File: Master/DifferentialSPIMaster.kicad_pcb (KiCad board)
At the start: 4 copper layers, 36 parts, among them J1 Motor Encoder 0, J2 Conn_01x20, J3 Motor Encoder 0, U1 MAX485E, U2 MAX485E, U3 MAX485E, U4 MAX485E, U5 MAX485E, U6 MAX485E

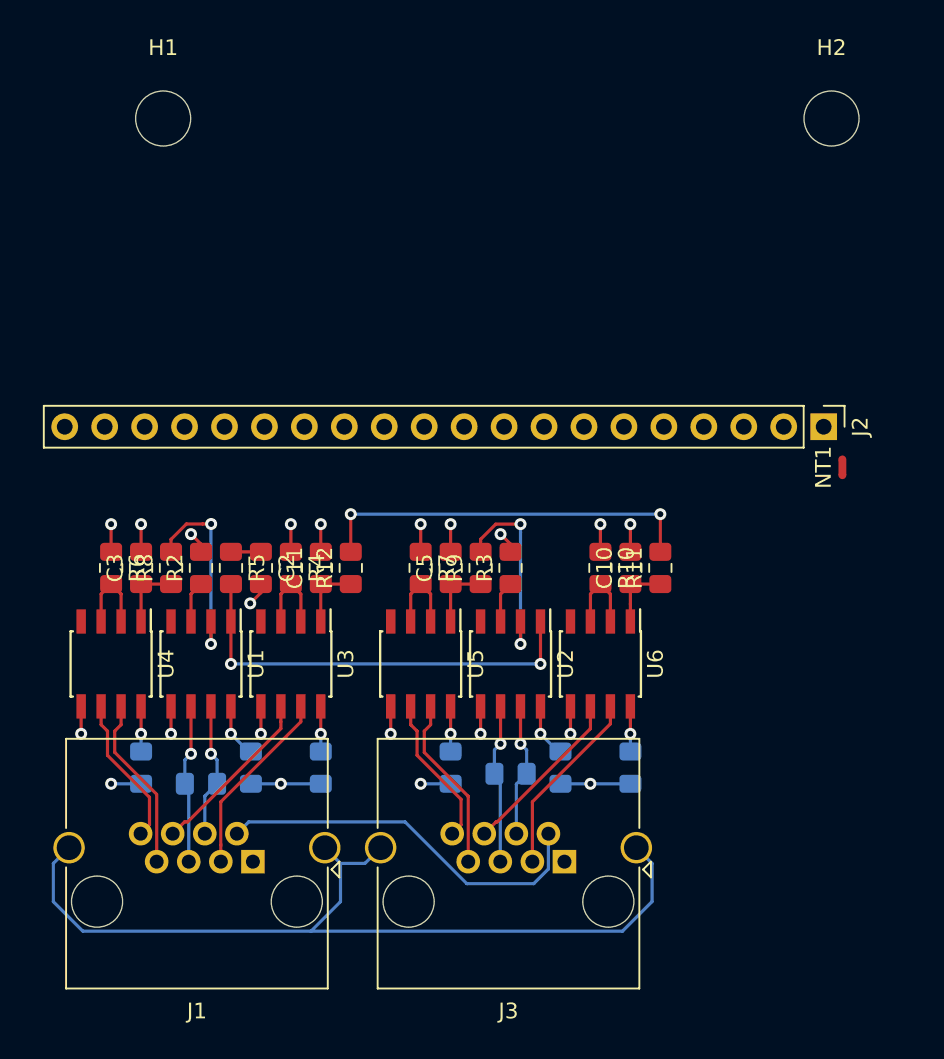
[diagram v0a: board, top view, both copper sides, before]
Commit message: CS transceivers now correctly setup to transmit, not receive
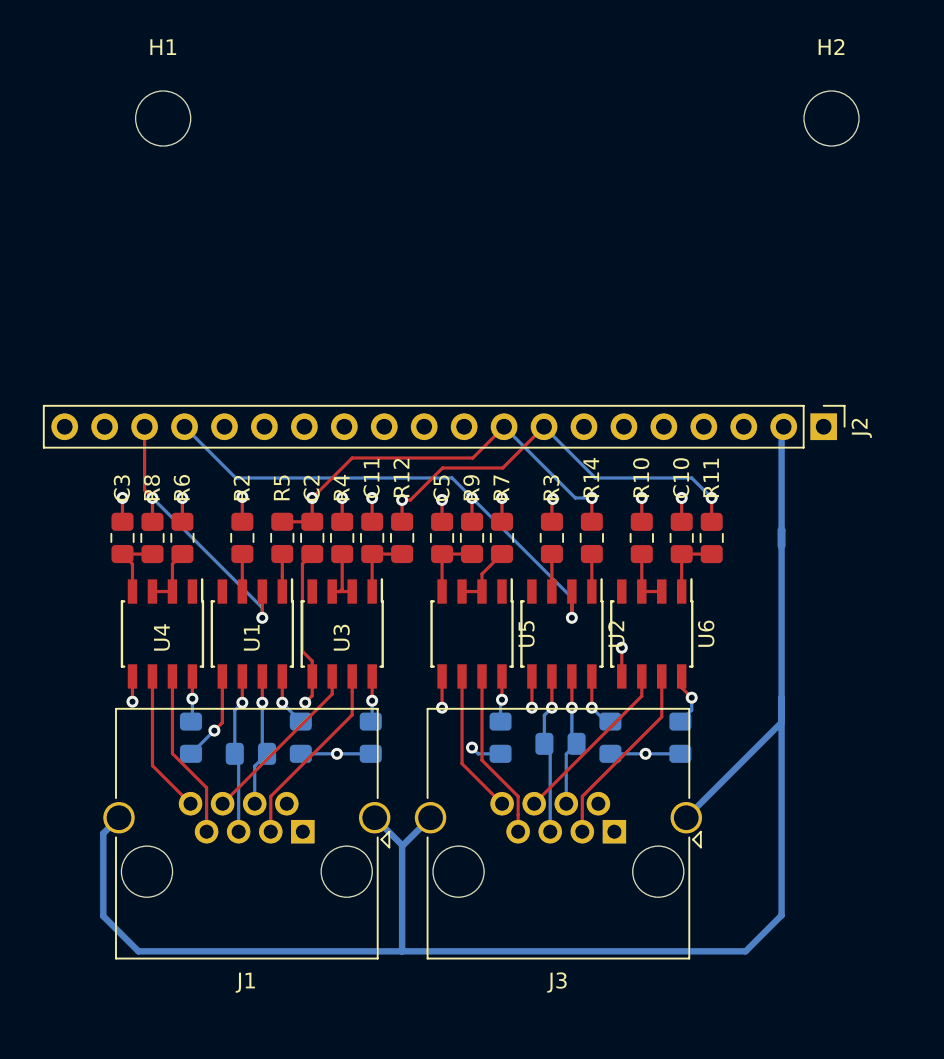
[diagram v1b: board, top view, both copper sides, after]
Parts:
- added R14: R, Resistor_SMD:R_0805_2012Metric_Pad1.15x1.40mm_HandSolder, F.Cu at (129.4, 96.6)
- NT1: moved to B.Cu
- moved NT1 5.92 mm to (141.5, 96.6)
- moved R7 5.51 mm to (123.7, 96.6)
- moved R6 4.92 mm to (103.4, 96.6)
- moved C11 3.78 mm to (115.4, 96.6)
- moved C2 3.78 mm to (111.6, 96.6)
- moved R12 3.78 mm to (117.3, 96.6)
- moved R5 3.78 mm to (109.7, 96.6)
- moved C10 3.78 mm to (135.1, 96.6)
- moved R11 3.78 mm to (137.0, 96.6)
- moved U6 3.78 mm to (133.2, 102.7)
- moved R4 3.78 mm to (113.5, 96.6)
- moved U1 3.78 mm to (107.8, 102.7)
- moved U2 3.78 mm to (127.5, 102.7)
- moved U3 3.78 mm to (113.5, 102.7)
- moved U4 3.78 mm to (102.1, 102.7)
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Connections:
- C1 pad 1: +3V3 -> +5V
- C2 pad 1: /MISO_ODRIVE -> /MISO
- C4 pad 1: +3V3 -> +5V
- C6 pad 1: +3V3 -> +5V
- C7 pad 1: +3V3 -> +5V
- C8 pad 1: +3V3 -> +5V
- C9 pad 1: +3V3 -> +5V
- J2 pad 1: Net-(J2-Pad1) -> +5V
- J2 pad 17: Net-(J2-Pad17) -> /CS_2
- J2 pad 18: Net-(J2-Pad18) -> /CS_1
- J2 pad 19: Net-(J2-Pad19) -> GNDD
- J2 pad 2: Net-(J2-Pad2) -> GNDD
- J2 pad 20: Net-(J2-Pad20) -> GNDD
- J2 pad 5: Net-(J2-Pad5) -> GNDD
- J2 pad 8: Net-(J2-Pad8) -> /SPI_SCK
- J2 pad 9: Net-(J2-Pad9) -> /MISO
- R10 pad 1: +3V3 -> +5V
- R11 pad 2: /CLK -> /SPI_SCK
- R12 pad 2: /CLK -> /SPI_SCK
- R4 pad 1: +3V3 -> +5V
- R5 pad 1: /MISO_ODRIVE -> /MISO
- R5 pad 2: /MISO -> Net-(R5-Pad2)
- R6 pad 1: +3V3 -> +5V
- R7 pad 1: +3V3 -> +5V
- U1 pad 1: /MISO -> Net-(R5-Pad2)
- U1 pad 8: +3V3 -> +5V
- U2 pad 1: /MISO -> Net-(R14-Pad2)
- U2 pad 8: +3V3 -> +5V
- U3 pad 8: +3V3 -> +5V
- U4 pad 1: Net-(C3-Pad1) -> Net-(U4-Pad1)
- U4 pad 4: Net-(U4-Pad4) -> Net-(C3-Pad1)
- U4 pad 8: +3V3 -> +5V
- U5 pad 1: Net-(C5-Pad1) -> Net-(U5-Pad1)
- U5 pad 4: Net-(U5-Pad4) -> Net-(C5-Pad1)
- U5 pad 8: +3V3 -> +5V
- U6 pad 8: +3V3 -> +5V
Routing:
- net GND: track 56.8 -> 97.1 mm
- net /SPI_SCK: track 0.00 -> 26.4 mm, vias 0 -> 2
- net +3V3: track 25.5 -> 0.00 mm, vias 10 -> 0
- net /CLK: track 24.5 -> 0.00 mm, vias 2 -> 0
- net /CS_2: track 12.8 -> 33.6 mm
- net GNDD: track 34.5 -> 49.8 mm, vias 17 -> 15
- net /CS_1: track 12.8 -> 18.4 mm
- net Net-(R5-Pad2): track 0.00 -> 2.39 mm
- net Net-(R14-Pad2): track 0.00 -> 2.39 mm
- net /MISO_ODRIVE: track 1.91 -> 0.00 mm
- net Net-(R10-Pad2): track 5.29 -> 3.65 mm
- net Net-(R6-Pad2): track 5.29 -> 3.92 mm
- net Net-(R7-Pad2): track 5.29 -> 4.18 mm
- net Net-(R4-Pad2): track 5.29 -> 4.21 mm
- net /MISO: track 27.5 -> 26.5 mm
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- added copper zone on In2.Cu, net +5V
- removed copper zone on In2.Cu, net +3V3

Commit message: CLK is an output, not an input on master, also add edge cuts layer
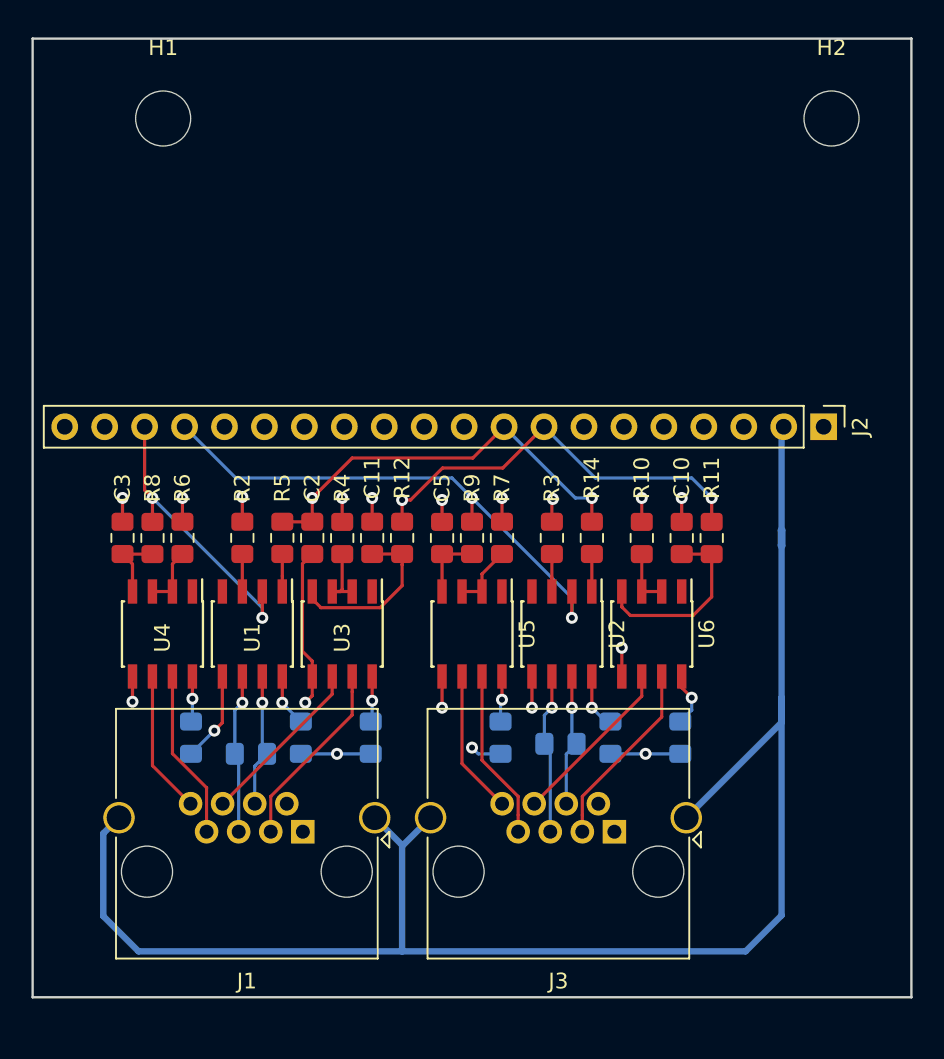
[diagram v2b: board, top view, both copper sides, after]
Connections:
- U3 pad 1: Net-(C11-Pad1) -> Net-(U3-Pad1)
- U3 pad 4: Net-(U3-Pad4) -> Net-(C11-Pad1)
- U6 pad 1: Net-(C10-Pad1) -> Net-(U6-Pad1)
- U6 pad 4: Net-(U6-Pad4) -> Net-(C10-Pad1)
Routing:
- net Net-(C10-Pad1): track 4.28 -> 12.0 mm
- net Net-(C11-Pad1): track 4.29 -> 10.9 mm
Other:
- board outline added: 55.9 x 61 mm
